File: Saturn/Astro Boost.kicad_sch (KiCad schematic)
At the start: 34 parts, among them J1 AudioJack2, J10 Power from SW to PS, J2 AudioJack2, J3 Jack-DC, J4 Signal In, J5 Audio In, J6 Processed to SW, J7 Bypass, J8 Processed Out, J9 Power from 9V to SW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

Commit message: Added Fix it list to jupiter
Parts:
- added J11: +9V, Connector_Wire:SolderWire-0.25sqmm_1x01_D0.65mm_OD2mm, symbol Connector_Generic:Conn_01x01
- added J12: -9V, Connector_Wire:SolderWire-0.25sqmm_1x01_D0.65mm_OD2mm, symbol Connector_Generic:Conn_01x01
- BT1: footprint Battery:BatteryHolder_Eagle_12BH611-GR -> 1_Custom:9V
- D2: footprint Capacitor_THT:C_Disc_D9.0mm_W5.0mm_P10.00mm -> Diode_THT:D_DO-34_SOD68_P7.62mm_Horizontal
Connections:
- net 0: now also J12.1 (Pin_1)
- net Power from 9V: now also J11.1 (Pin_1)
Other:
- note removed: "Add pos/neg for electrolytic caps and d1/d2 use different filter caps, these are huge flip c7 so it matches widen r5,r4, r2 u1 footprint too wide r3 holes too small Q1 leads too close together move power jack to other side"
- note removed: "link datasheets"
- moved on the sheet: BT1, J3

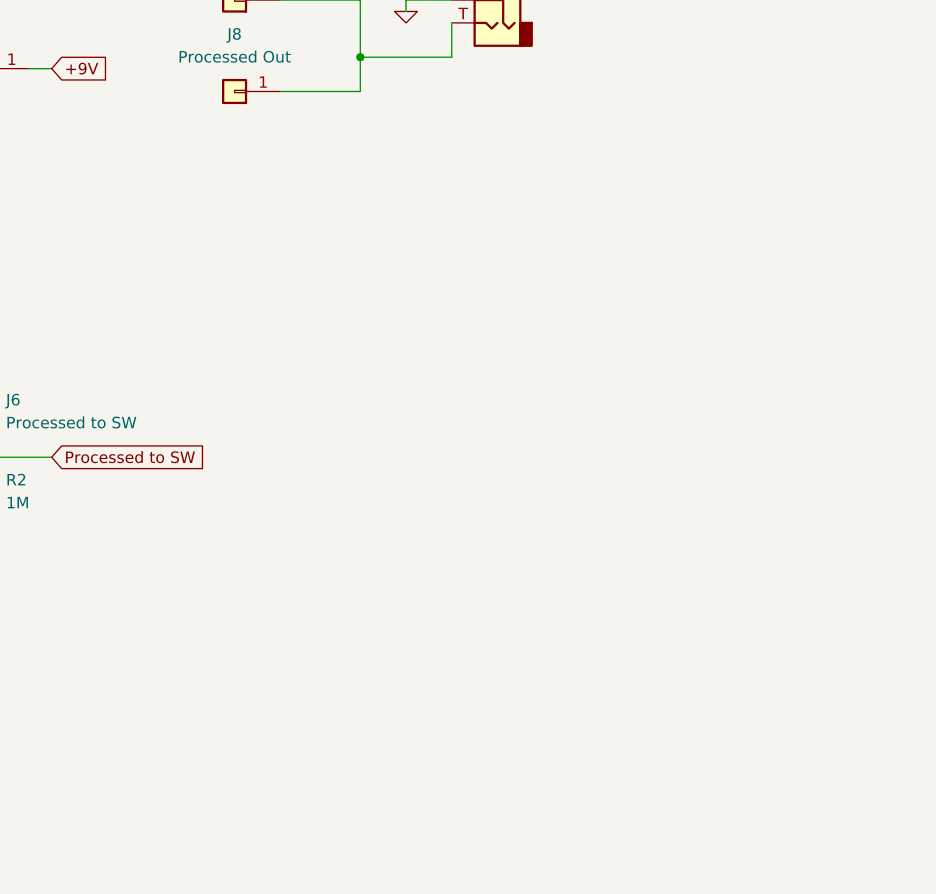
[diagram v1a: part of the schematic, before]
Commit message: Updates to Saturn
Removed wiring pads and associated tracks
Added to do list
Shortened PCB
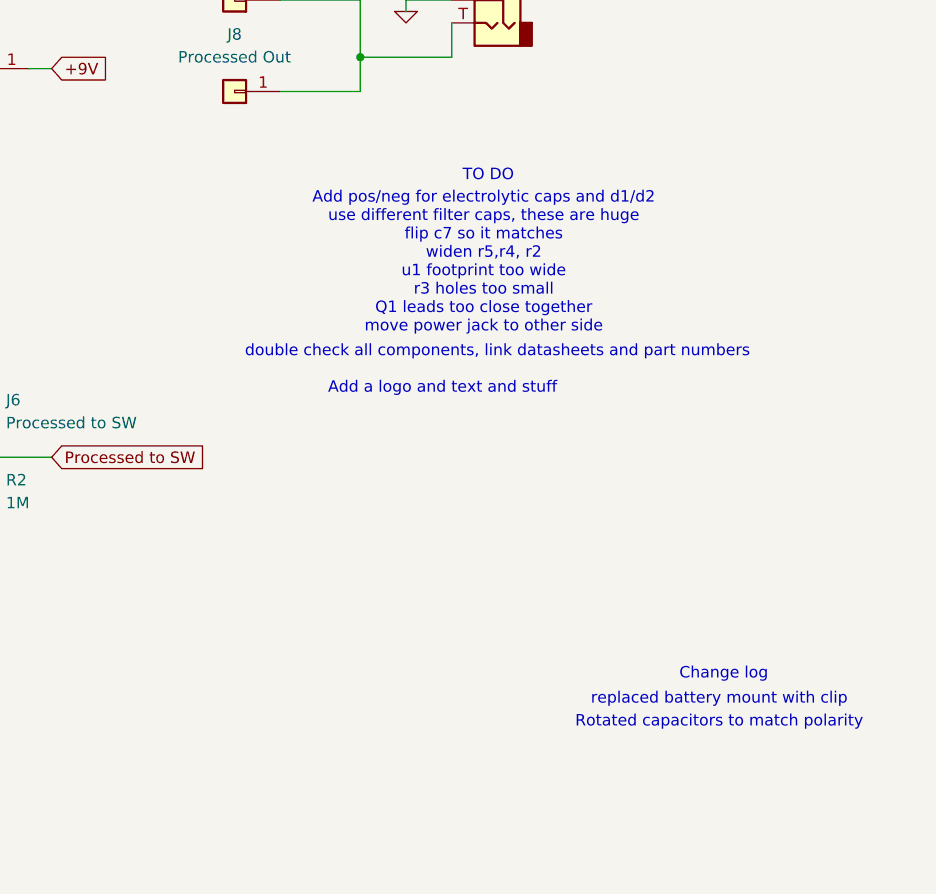
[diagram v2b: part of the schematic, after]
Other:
- note added: "Add a logo and text and stuff"
- note added: "Add pos/neg for electrolytic caps and d1/d2 use different filter caps, these are huge flip c7 so it matches widen r5,r4, r2 u1 footprint too wide r3 holes too small Q1 leads too close together move power jack to other side"
- note added: "Change log"
- note added: "Rotated capacitors to match polarity"
- note added: "TO DO"
- note added: "double check all components, link datasheets and part numbers"
- note added: "replaced battery mount with clip"
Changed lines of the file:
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@@
+		)
+	)
+	(text "TO DO"
+		(exclude_from_sim no)
+		(at 223.774 57.658 0)
+		(effects
+			(font
+				(size 1.27 1.27)
+			)
+		)
+	)
+	(text "double check all components, link datasheets and part numbers"
+		(exclude_from_sim no)
+		(at 224.79 77.216 0)
+		(effects
+			(font
+				(size 1.27 1.27)
+			)
+		)
+	)
+	(text "Change log"
+		(exclude_from_sim no)
+		(at 249.936 113.03 0)
+		(effects
+			(font
+				(size 1.27 1.27)
+			)
+		)
+	)
+	(text "replaced battery mount with clip"
+		(exclude_from_sim no)
+		(at 249.428 115.824 0)
+		(effects
+			(font
+				(size 1.27 1.27)
+			)
 		)
 	)
@@
 		(effects
 			(font
+				(size 1.27 1.27)
+			)
+		)
+	)
+	(text "Add pos/neg for electrolytic caps and d1/d2\nuse different filter caps, these are huge\nflip c7 so it matches\nwiden r5,r4, r2\nu1 footprint too wide\nr3 holes too small\nQ1 leads too close together\nmove power jack to other side"
+		(exclude_from_sim no)
+		(at 223.266 67.31 0)
+		(effects
+			(font
+				(size 1.27 1.27)
+			)
+		)
+	)
+	(text "Add a logo and text and stuff"
+		(exclude_from_sim no)
+		(at 218.694 81.28 0)
+		(effects
+			(font
+				(size 1.27 1.27)
+			)
+		)
+	)
+	(text "Rotated capacitors to match polarity"
+		(exclude_from_sim no)
+		(at 249.428 118.364 0)
+		(effects
+			(font
